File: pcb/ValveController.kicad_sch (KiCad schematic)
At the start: 72 parts, among them J10 1770966, J11 1770966, J12 1770966, J13 USB4115-03-C, J14 1770966, J2 1990986, J3 1990986, J8 1770966, J9 1770966, Q3 MOC3063S-TA1, Q4 MOC3063S-TA1, Q5 CSD17313Q2, SW1 TL9320AF400QG, U1 IRM-03-5, U2 TLV75733P, U5 ESP32-C6-WROOM-1-N4, U6 TPS61040

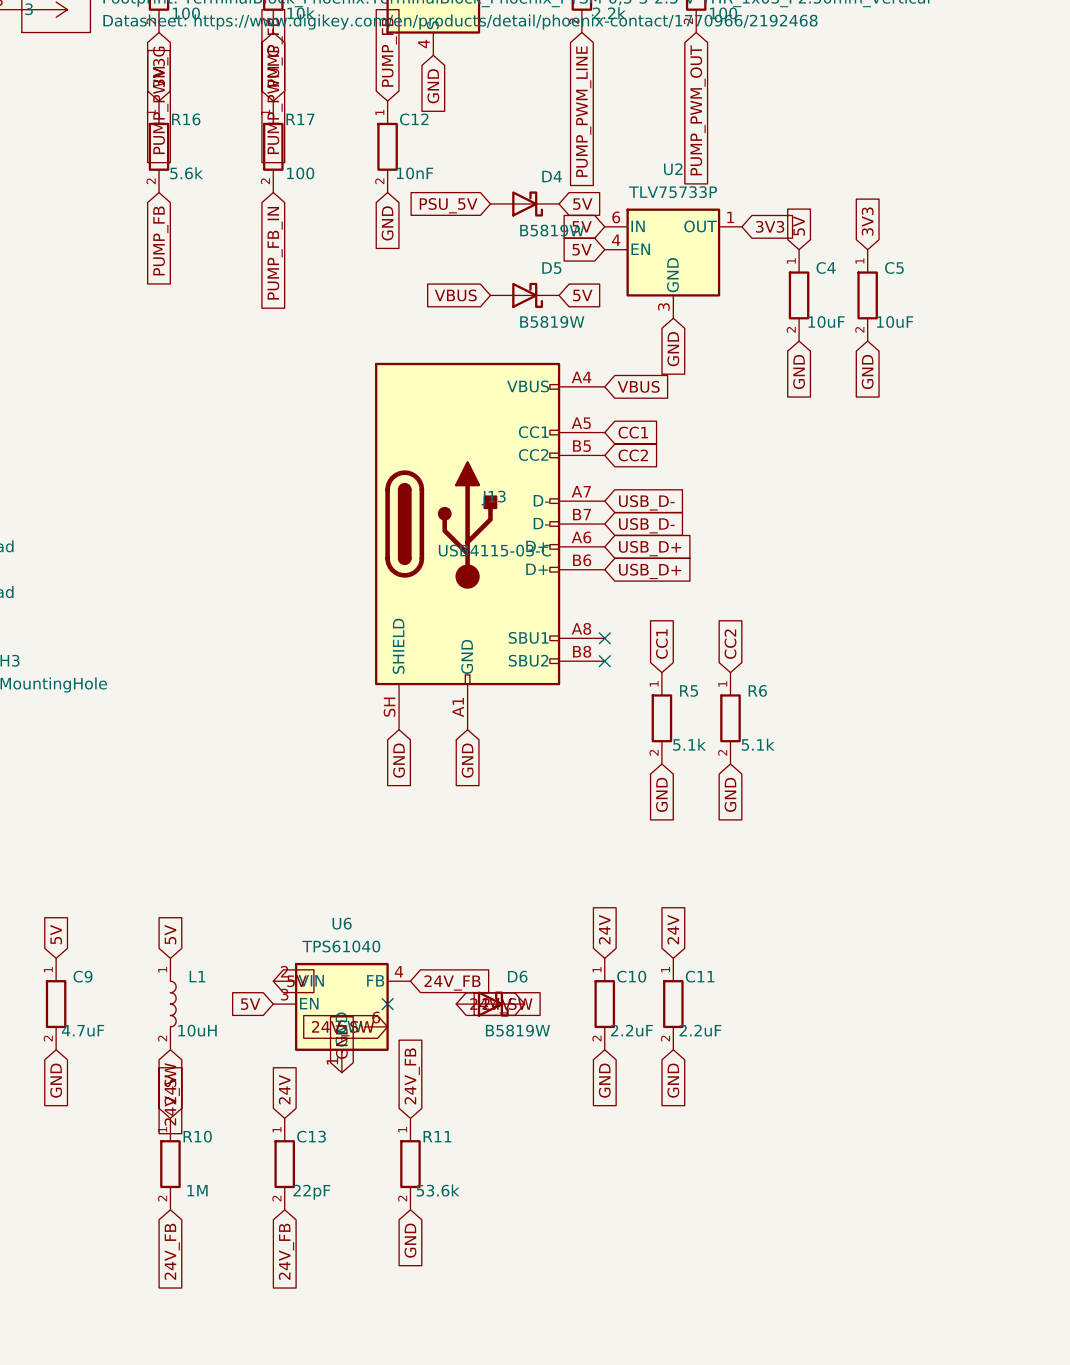
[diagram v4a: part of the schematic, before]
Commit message: fix(pcb): 24V rail Zener clamp, FB divider rescale, R16 10k, Q5 pin7 name (final review)
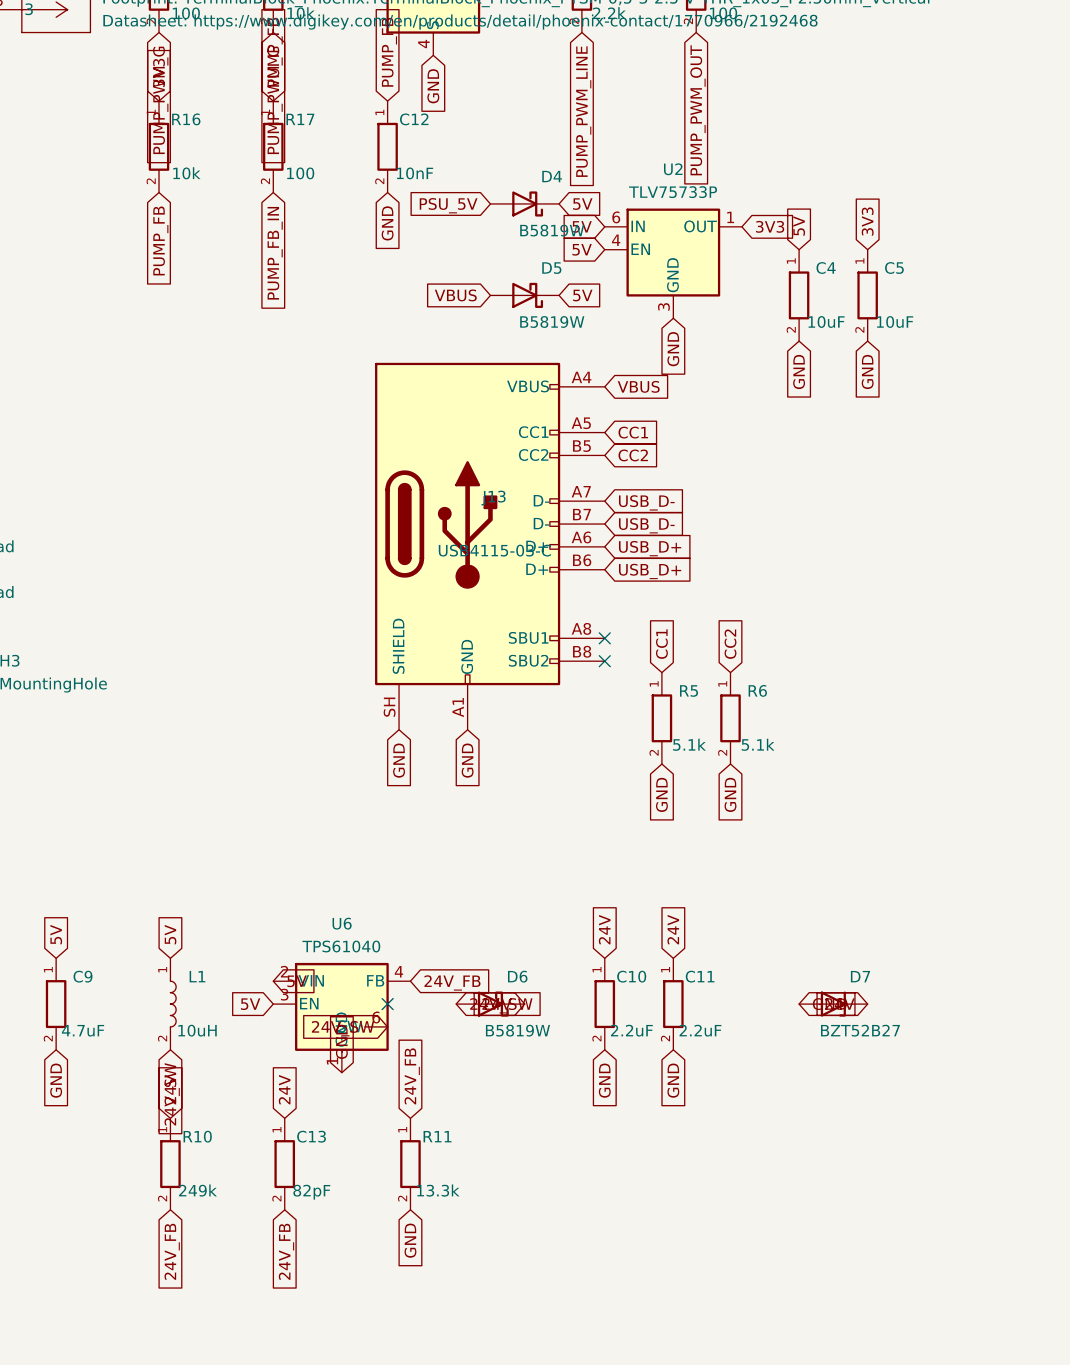
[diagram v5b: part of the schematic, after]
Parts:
- added D7: BZT52B27, Diode_SMD:D_SOD-123F, symbol Device:D_Zener
- C13: value 22pF -> 82pF; DigiKey https://www.digikey.com/en/products/detail/murata-electronics/GRM1555C1H220JA01D/3175187 -> https://www.digikey.com/en/products/detail/murata-electronics/GRM1555C1H820JA01D/3175198; MPN GRM1555C1H220JA01D -> GRM1555C1H820JA01D
- R10: value 1M -> 249k; DigiKey https://www.digikey.com/en/products/detail/yageo/RC0402FR-071ML/726515 -> https://www.digikey.com/en/products/detail/yageo/RC0402FR-07249KL/726570; MPN RC0402FR-071ML -> RC0402FR-07249KL
- R11: value 53.6k -> 13.3k; DigiKey https://www.digikey.com/en/products/detail/yageo/RC0402FR-0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 -> https://www.digikey.com/en/products/result?keywords=RC0402F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; MPN RC0402FR-0753K6L -> RC0402FR-0713K3L
- R16: value 5.6k -> 10k; DigiKey https://www.digikey.com/en/products/detail/yageo/RC0402FR-0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 -> https://www.digikey.com/en/products/detail/yageo/AC0402FR-0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; MPN RC0402FR-075K6L -> AC0402FR-0710KL
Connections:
- net 24V: now also D7.1 (K)
- net GND: now also D7.2 (A)
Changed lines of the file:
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@@
+	)
+	(symbol
+		(lib_id "Device:D_Zener")
+		(at 335.28 213.36 180)
+		(unit 1)
+		(body_style 1)
+		(exclude_from_sim no)
+		(in_bom yes)
+		(on_board yes)
+		(in_pos_files yes)
+		(dnp no)
+		(property "Reference" "D7"
+			(at 338.28 210.36 0)
+			(show_name no)
+			(do_not_autoplace no)
+			(effects
+				(font
+					(size 1.27 1.27)
+				)
+			)
+		)
+		(property "Value" "BZT52B27"
+			(at 338.28 216.36 0)
+			(show_name no)
+			(do_not_autoplace no)
+			(effects
+				(font
+					(size 1.27 1.27)
+				)
+			)
+		)
+		(property "Footprint" "Diode_SMD:D_SOD-123F"
+			(at 335.28 213.36 0)
+			(show_name no)
+			(do_not_autoplace no)
+			(hide yes)
+			(effects
+				(font
+					(size 1.27 1.27)
+				)
+			)
+		)
+		(property "Datasheet" "https://diotec.com/request/datasheet/bzt52b2v4.pdf"
+			(at 335.28 213.36 0)
+			(show_name no)
+			(do_not_autoplace no)
+			(hide yes)
+			(effects
+				(font
+					(size 1.27 1.27)
+				)
+			)
+		)
+		(property "Description" "24V rail Zener clamp (FB-open fault protection, TPS61040 has no internal OVP)"
+			(at 335.28 213.36 0)
+			(show_name no)
+			(do_not_autoplace no)
+			(hide yes)
+			(effects
+				(font
+					(size 1.27 1.27)
+				)
+			)
+		)
+		(property "MPN" "BZT52B27"
+			(at 335.28 213.36 0)
+			(show_name no)
+			(do_not_autoplace no)
+			(hide yes)
+			(effects
+				(font
+					(size 1.27 1.27)
+				)
+			)
+		)
+		(property "DigiKey" "https://www.digikey.com/en/products/detail/diotec-semiconductor/BZT52B27/22191724"
+			(at 335.28 213.36 0)
+			(show_name no)
+			(do_not_autoplace no)
+			(hide yes)
+			(effects
+				(font
+					(size 1.27 1.27)
+				)
+			)
+		)
+		(pin "1"
+		)
+		(pin "2"
+		)
+		(instances
+			(project "ValveController"
+				(path "/996e7a69-443b-4feb-9505-1512f377356d"
+					(reference "D7")
+					(unit 1)
+				)
+			)
+		)
 	)
 	(symbol
@@
 			)
 		)
-		(property "Value" "1M"
+		(property "Value" "249k"
 			(at 264.62 234.14 0)
 			(show_name no)
@@
 			)
 		)
-		(property "MPN" "RC0402FR-071ML"
+		(property "MPN" "RC0402FR-07249KL"
 			(at 261.62 231.14 0)
 			(show_name no)
@@
 			)
 		)
-		(property "DigiKey" "https://www.digikey.com/en/products/detail/yageo/RC0402FR-071ML/726515"
+		(property "DigiKey" "https://www.digikey.com/en/products/detail/yageo/RC0402FR-07249KL/726570"
 			(at 261.62 231.14 0)
 			(show_name no)
@@
 			)
 		)
-		(property "Value" "22pF"
+		(property "Value" "82pF"
 			(at 277.32 234.14 0)
 			(show_name no)
@@
 			)
 		)
-		(property "MPN" "GRM1555C1H220JA01D"
+		(property "MPN" "GRM1555C1H820JA01D"
 			(at 274.32 231.14 0)
 			(show_name no)
@@
 			)
 		)
-		(property "DigiKey" "https://www.digikey.com/en/products/detail/murata-electronics/GRM1555C1H220JA01D/3175187"
+		(property "DigiKey" "https://www.digikey.com/en/products/detail/murata-electronics/GRM1555C1H820JA01D/3175198"
 			(at 274.32 231.14 0)
 			(show_name no)
@@
 			)
 		)
-		(property "Value" "53.6k"
+		(property "Value" "13.3k"
 			(at 291.29 234.14 0)
 			(show_name no)
@@
 			)
 		)
-		(property "MPN" "RC0402FR-0753K6L"
+		(property "MPN" "RC0402FR-0713K3L"
 			(at 288.29 231.14 0)
 			(show_name no)
@@
 			)
 		)
-		(property "DigiKey" "https://www.digikey.com/en/products/detail/yageo/RC0402FR-0753K6L/726634"
+		(property "DigiKey" "https://www.digikey.com/en/products/result?keywords=RC0402FR-0713K3L"
 			(at 288.29 231.14 0)
 			(show_name no)
@@
 		(shape input)
 		(at 293.37 213.36 0)
+		(effects
+			(font
+				(size 1.27 1.27)
+			)
+			(justify left)
+		)
+		(property "Intersheetrefs" "${INTERSHEET_REFS}"
+			(at 182.88 266.7 0)
+			(hide yes)
+			(show_name no)
+			(do_not_autoplace no)
+			(effects
+				(font
+					(size 1.27 1.27)
+				)
+			)
+		)
+	)
+	(global_label "24V"
+		(shape input)
+		(at 339.09 213.36 180)
+		(effects
+			(font
+				(size 1.27 1.27)
+			)
+			(justify right)
+		)
+		(property "Intersheetrefs" "${INTERSHEET_REFS}"
+			(at 182.88 266.7 0)
+			(hide yes)
+			(show_name no)
+			(do_not_autoplace no)
+			(effects
+				(font
+					(size 1.27 1.27)
+				)
+			)
+		)
+	)
+	(global_label "GND"
+		(shape input)
+		(at 331.47 213.36 0)
 		(effects
 			(font
@@
 			)
 		)
-		(property "Value" "5.6k"
+		(property "Value" "10k"
 			(at 263.35 121.11 0)
 			(show_name no)
@@
 			)
 		)
-		(property "MPN" "RC0402FR-075K6L"
+		(property "MPN" "AC0402FR-0710KL"
 			(at 260.35 118.11 0)
 			(show_name no)
@@
 			)
 		)
-		(property "DigiKey" "https://www.digikey.com/en/products/detail/yageo/RC0402FR-075K6L/2827590"
+		(property "DigiKey" "https://www.digikey.com/en/products/detail/yageo/AC0402FR-0710KL/5895030"
 			(at 260.35 118.11 0)
 			(show_name no)

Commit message: feat(pcb): 8x8 matrix display, I2C driver, page button
Add U7 (IS31FL3730 I2C LED matrix driver, hand-embedded QFN-24 symbol)
and DS1 (KWM-20881AGB 8x8 row-anode dot matrix, new THT footprint),
wired via I2C_SDA/I2C_SCL with R18/R19 pull-ups and U7 decoupling
(C14 100nF + C15 1uF bulk). SW2 adds a page-cycle button on BTN_PAGE.
U7.SDB hard-tied to 3V3 (no GPIO allocated for hardware shutdown).
Frees U5's IO6/IO7/IO11 no-connect markers for the new nets.
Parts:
- added C14: 100nF, Capacitor_SMD:C_0402_1005Metric, symbol C_dev
- added C15: 1uF, Capacitor_SMD:C_0402_1005Metric, symbol C_dev
- added DS1: KWM-20881AGB, Kleist2:LED_Matrix_8x8_20mm, symbol Kleist:KWM-20881AGB
- added R18, R19: 4.7k, Resistor_SMD:R_0402_1005Metric, symbol R_dev
- added SW2: TL9320AF400QG, Kleist2:SW_SPST_TL9320, symbol Switch:SW_Push
- added U7: IS31FL3730, Package_DFN_QFN:QFN-24-1EP_4x4mm_P0.5mm_EP2.5x2.5mm, symbol Kleist:IS31FL3730
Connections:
- net 3V3: now also C14.1, C15.1, R18.1, R19.1, U7.11 (VCC), U7.3 (SDB)
- net GND: now also C14.2, C15.2, SW2.2, U7.20 (GND), U7.25 (GND), U7.4 (IN), U7.5 (C_FILT), U7.6 (AD)
- net BTN_PAGE: now reaches U5.12 (IO11)
- net BTN_PAGE: now also SW2.1
- net I2C_SDA: now reaches U5.6 (IO6)
- net I2C_SDA: now also R18.2, U7.1 (SDA)
- net I2C_SCL: now reaches U5.7 (IO7)
- net I2C_SCL: now also R19.2, U7.2 (SCL)
- new net DISP_C1: DS1.13 (COL1), U7.24 (C1)
- new net DISP_C2: DS1.3 (COL2), U7.23 (C2)
- new net DISP_C3: DS1.4 (COL3), U7.22 (C3)
- new net DISP_C4: DS1.10 (COL4), U7.21 (C4)
- new net DISP_C5: DS1.6 (COL5), U7.19 (C5)
- new net DISP_C6: DS1.11 (COL6), U7.18 (C6)
- new net DISP_C7: DS1.15 (COL7), U7.17 (C7)
- new net DISP_C8: DS1.16 (COL8), U7.16 (C8)
- new net DISP_R1: DS1.9 (ROW1), U7.7 (R1)
- new net DISP_R2: DS1.14 (ROW2), U7.8 (R2)
- new net DISP_R3: DS1.8 (ROW3), U7.9 (R3)
- new net DISP_R4: DS1.12 (ROW4), U7.10 (R4)
- new net DISP_R5: DS1.1 (ROW5), U7.12 (R5)
- new net DISP_R6: DS1.7 (ROW6), U7.13 (R6/C11)
- new net DISP_R7: DS1.2 (ROW7), U7.14 (R7/C10)
- new net DISP_R8: DS1.5 (ROW8), U7.15 (R8/C9)
- no-connect marks 16 -> 13

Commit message: feat(pcb): 2x isolated 24VAC aux PhotoMOS channels, J15
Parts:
- added J15: 1770979, TerminalBlock_Phoenix:TerminalBlock_Phoenix_PTSM-0,5-4-2.5-V-THR_1x04_P2.50mm_Vertical, symbol Kleist:1770979
- added Q6, Q7: CPC1017N, Package_SO:SOP-4_3.8x4.1mm_P2.54mm, symbol Relay_SolidState:CPC1017N
- added R20, R21: 10k, Resistor_SMD:R_0402_1005Metric, symbol R_dev
- added RL3, RL4: 680, Resistor_SMD:R_0402_1005Metric, symbol R_dev
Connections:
- net GND: now also Q6.2, Q7.2, R20.2, R21.2
- net AUX1_EN: now reaches U5.20 (IO22)
- net AUX1_EN: now also R20.1, RL3.1
- net AUX2_EN: now reaches U5.21 (IO23)
- net AUX2_EN: now also R21.1, RL4.1
- new net AUX1_DRV: Q6.1, RL3.2
- new net AUX1_IN: J15.1, Q6.4
- new net AUX1_OUT: J15.2, Q6.3
- new net AUX2_DRV: Q7.1, RL4.2
- new net AUX2_IN: J15.3, Q7.4
- new net AUX2_OUT: J15.4, Q7.3
- no-connect marks 13 -> 11
